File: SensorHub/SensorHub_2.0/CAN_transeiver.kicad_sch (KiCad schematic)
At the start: 4 parts, among them U3 TJA1051TK-3

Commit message: TCAN334
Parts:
- removed U3: TJA1051TK-3, Package_SON:HVSON-8-1EP_3x3mm_P0.65mm_EP1.6x2.4mm, symbol Interface_CAN_LIN:TJA1051TK-3
- added U9: TCAN334, Package_TO_SOT_SMD:TSOT-23-8_HandSoldering, symbol Interface_CAN_LIN:TCAN334
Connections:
- net +3.3V: now also U9.3 (VCC)
- net Can_H: now also U9.7 (CANH)
- net Can_L: now also U9.6 (CANL)
- net GND: now also U9.2 (GND), U9.5 (SHDN), U9.8 (STB)
- net RXD: now also U9.4 (RXD)
- net TXD: now also U9.1 (TXD)
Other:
- note removed: "CAN transceiver"
- moved on the sheet: C4, R13, R14

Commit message: TCAN334
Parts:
- removed U9: TCAN334, Package_TO_SOT_SMD:TSOT-23-8_HandSoldering, symbol Interface_CAN_LIN:TCAN334
- added U3: TCAN334, Package_TO_SOT_SMD:TSOT-23-8, symbol Interface_CAN_LIN:TCAN334
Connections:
- net +3.3V: now also U3.3 (VCC)
- net Can_H: now also U3.7 (CANH)
- net Can_L: now also U3.6 (CANL)
- net GND: now also U3.2 (GND), U3.5 (SHDN), U3.8 (STB)
- net RXD: now also U3.4 (RXD)
- net TXD: now also U3.1 (TXD)
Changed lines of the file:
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@@
+	)
+	(junction
+		(at 118.11 90.17)
+		(diameter 0)
+		(color 0 0 0 0)
+	)
+	(junction
+		(at 149.86 107.95)
+		(diameter 0)
+		(color 0 0 0 0)
 	)
 	(junction
@@
 		(color 0 0 0 0)
 	)
-	(junction
-		(at 149.86 107.95)
-		(diameter 0)
-		(color 0 0 0 0)
-	)
-	(junction
-		(at 118.11 90.17)
-		(diameter 0)
-		(color 0 0 0 0)
-	)
 	(wire
 		(pts
@@
 	(wire
 		(pts
+			(xy 149.86 107.95) (xy 149.86 113.03)
+		)
+		(stroke
+			(width 0)
+			(type default)
+		)
+	)
+	(wire
+		(pts
 			(xy 110.49 90.17) (xy 110.49 99.06)
 		)
@@
 	(wire
 		(pts
+			(xy 127 90.17) (xy 118.11 90.17)
+		)
+		(stroke
+			(width 0)
+			(type default)
+		)
+	)
+	(wire
+		(pts
+			(xy 110.49 116.84) (xy 110.49 106.68)
+		)
+		(stroke
+			(width 0)
+			(type default)
+		)
+	)
+	(wire
+		(pts
+			(xy 162.56 114.3) (xy 162.56 113.03)
+		)
+		(stroke
+			(width 0)
+			(type default)
+		)
+	)
+	(wire
+		(pts
 			(xy 149.86 105.41) (xy 149.86 107.95)
-		)
-		(stroke
-			(width 0)
-			(type default)
-		)
-	)
-	(wire
-		(pts
-			(xy 127 90.17) (xy 118.11 90.17)
-		)
-		(stroke
-			(width 0)
-			(type default)
-		)
-	)
-	(wire
-		(pts
-			(xy 149.86 107.95) (xy 149.86 113.03)
-		)
-		(stroke
-			(width 0)
-			(type default)
-		)
-	)
-	(wire
-		(pts
-			(xy 110.49 116.84) (xy 110.49 106.68)
-		)
-		(stroke
-			(width 0)
-			(type default)
-		)
-	)
-	(wire
-		(pts
-			(xy 162.56 114.3) (xy 162.56 113.03)
 		)
 		(stroke
@@
 	)
 	(symbol
-		(lib_id "Interface_CAN_LIN:TCAN334")
-		(at 162.56 102.87 0)
-		(unit 1)
-		(exclude_from_sim no)
-		(in_bom yes)
-		(on_board yes)
-		(dnp no)
-		(fields_autoplaced yes)
-		(property "Reference" "U9"
-			(at 164.7033 90.17 0)
-			(effects
-				(font
-					(size 1.27 1.27)
-				)
-				(justify left)
-			)
-		)
-		(property "Value" "TCAN334"
-			(at 164.7033 92.71 0)
-			(effects
-				(font
-					(size 1.27 1.27)
-				)
-				(justify left)
-			)
-		)
-		(property "Footprint" "Package_TO_SOT_SMD:TSOT-23-8_HandSoldering"
-			(at 162.56 115.57 0)
-			(effects
-				(font
-					(size 1.27 1.27)
-					(italic yes)
-				)
-				(hide yes)
-			)
-		)
-		(property "Datasheet" "http://www.ti.com/lit/ds/symlink/tcan337.pdf"
-			(at 162.56 102.87 0)
-			(effects
-				(font
-					(size 1.27 1.27)
-				)
-				(hide yes)
-			)
-		)
-		(property "Description" "High-Speed CAN Transceiver, 1Mbps, 3.3V supply, low power standby mode, shutdown mode, SOT-23-8/SOIC-8"
-			(at 162.56 102.87 0)
-			(effects
-				(font
-					(size 1.27 1.27)
-				)
-				(hide yes)
-			)
-		)
-		(pin "4"
-		)
-		(pin "7"
-		)
-		(pin "1"
-		)
-		(pin "5"
-		)
-		(pin "3"
-		)
-		(pin "6"
-		)
-		(pin "8"
-		)
-		(pin "2"
-		)
-		(instances
-			(project "SensorHub_2.0"
-				(path "/9668bc71-8924-498e-982f-628f3083c8b8/aeef27da-d3bb-47bb-8fd5-6871969d5416"
-					(reference "U9")
-					(unit 1)
-				)
-			)
-		)
-	)
-	(symbol
 		(lib_id "Device:R")
 		(at 118.11 102.87 0)
@@
 					(unit 1)
 				)
+			)
+		)
+	)
+	(symbol
+		(lib_id "Interface_CAN_LIN:TCAN334")
+		(at 162.56 102.87 0)
+		(unit 1)
+		(exclude_from_sim no)
+		(in_bom yes)
+		(on_board yes)
+		(dnp no)
+		(fields_autoplaced yes)
+		(property "Reference" "U3"
+			(at 164.7033 90.17 0)
+			(effects
+				(font
+					(size 1.27 1.27)
+				)
+				(justify left)
+			)
+		)
+		(property "Value" "TCAN334"
+			(at 164.7033 92.71 0)
+			(effects
+				(font
+					(size 1.27 1.27)
+				)
+				(justify left)
+			)
+		)
+		(property "Footprint" "Package_TO_SOT_SMD:TSOT-23-8"
+			(at 162.56 115.57 0)
+			(effects
+				(font
+					(size 1.27 1.27)
+					(italic yes)
+				)
+				(hide yes)
+			)
+		)
+		(property "Datasheet" "http://www.ti.com/lit/ds/symlink/tcan337.pdf"
+			(at 162.56 102.87 0)
+			(effects
+				(font
+					(size 1.27 1.27)
+				)
+				(hide yes)
+			)
+		)
+		(property "Description" "High-Speed CAN Transceiver, 1Mbps, 3.3V supply, low power standby mode, shutdown mode, SOT-23-8/SOIC-8"
+			(at 162.56 102.87 0)
+			(effects
+				(font
+					(size 1.27 1.27)
+				)
+				(hide yes)
+			)
+		)
+		(pin "3"
+		)
+		(pin "5"
+		)
+		(pin "1"
+		)
+		(pin "4"
+		)
+		(pin "2"
+		)
+		(pin "8"
+		)
+		(pin "7"
+		)
+		(pin "6"
+		)
+		(instances
+			(project "SensorHub_2.0"
+				(path "/9668bc71-8924-498e-982f-628f3083c8b8/aeef27da-d3bb-47bb-8fd5-6871969d5416"
+					(reference "U3")
+					(unit 1)
+				)

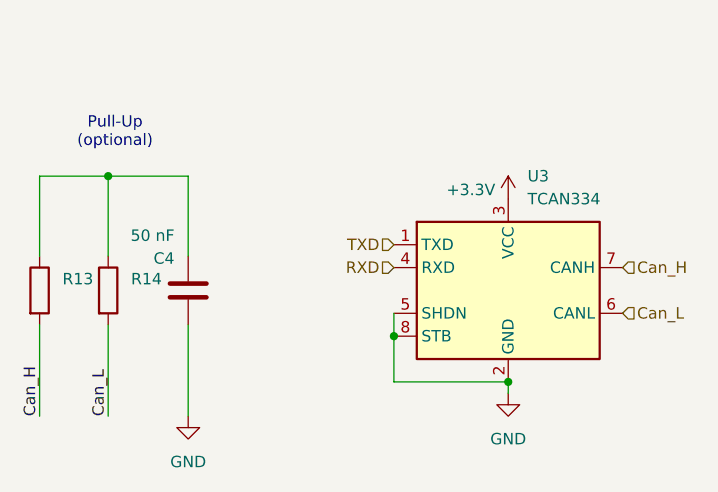
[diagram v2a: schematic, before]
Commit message: 32k oscillator
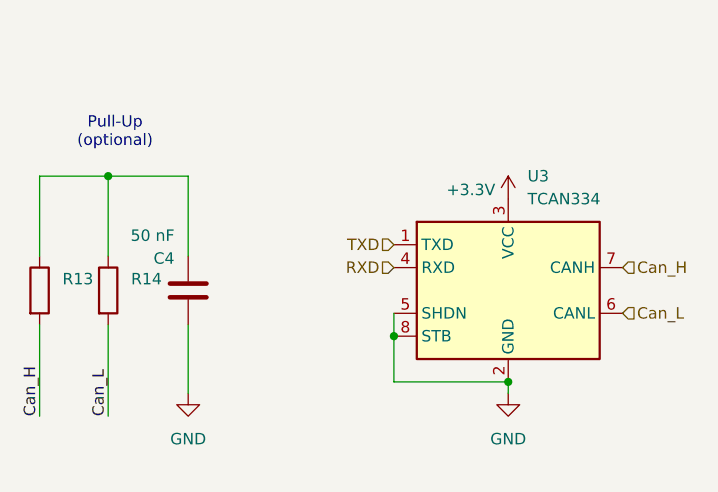
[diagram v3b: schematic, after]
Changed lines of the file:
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@@
 	(wire
 		(pts
-			(xy 127 106.68) (xy 127 116.84)
+			(xy 127 106.68) (xy 127 114.3)
 		)
 		(stroke
@@
 	(symbol
 		(lib_id "power:GND")
-		(at 127 116.84 0)
+		(at 127 114.3 0)
 		(unit 1)
 		(exclude_from_sim no)
@@
 		(fields_autoplaced yes)
 		(property "Reference" "#PWR016"
-			(at 127 123.19 0)
+			(at 127 120.65 0)
 			(effects
 				(font
@@
 		)
 		(property "Value" "GND"
-			(at 127 121.92 0)
+			(at 127 119.38 0)
 			(effects
 				(font
@@
 		)
 		(property "Footprint" ""
-			(at 127 116.84 0)
+			(at 127 114.3 0)
 			(effects
 				(font
@@
 		)
 		(property "Datasheet" ""
-			(at 127 116.84 0)
+			(at 127 114.3 0)
 			(effects
 				(font
@@
 		)
 		(property "Description" "Power symbol creates a global label with name \"GND\" , ground"
-			(at 127 116.84 0)
+			(at 127 114.3 0)
 			(effects
 				(font

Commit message: Vesrion 2
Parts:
- added R16: 10k, Resistor_SMD:R_0201_0603Metric, symbol Device:R
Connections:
- net GND: now also R16.1; no longer U3.5 (SHDN), U3.8 (STB)
- new net: R16.2, U3.5 (SHDN)
- new net STB: U3.8 (STB)
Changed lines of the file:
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@@
 		(color 0 0 0 0)
 	)
-	(junction
-		(at 149.86 107.95)
-		(diameter 0)
-		(color 0 0 0 0)
-	)
-	(junction
-		(at 162.56 113.03)
-		(diameter 0)
-		(color 0 0 0 0)
-	)
 	(wire
 		(pts
@@
 	(wire
 		(pts
-			(xy 149.86 107.95) (xy 149.86 113.03)
-		)
-		(stroke
-			(width 0)
-			(type default)
-		)
-	)
-	(wire
-		(pts
 			(xy 110.49 90.17) (xy 110.49 99.06)
 		)
@@
 	(wire
 		(pts
-			(xy 149.86 113.03) (xy 162.56 113.03)
+			(xy 144.78 105.41) (xy 149.86 105.41)
 		)
 		(stroke
@@
 	(wire
 		(pts
-			(xy 162.56 114.3) (xy 162.56 113.03)
-		)
-		(stroke
-			(width 0)
-			(type default)
-		)
-	)
-	(wire
-		(pts
-			(xy 149.86 105.41) (xy 149.86 107.95)
+			(xy 135.89 105.41) (xy 137.16 105.41)
 		)
 		(stroke
@@
 			)
 			(justify left bottom)
+		)
+	)
+	(hierarchical_label "STB"
+		(shape input)
+		(at 149.86 107.95 180)
+		(effects
+			(font
+				(size 1.27 1.27)
+			)
+			(justify right)
 		)
 	)
@@
 	)
 	(symbol
+		(lib_id "Device:R")
+		(at 140.97 105.41 90)
+		(unit 1)
+		(exclude_from_sim no)
+		(in_bom yes)
+		(on_board yes)
+		(dnp no)
+		(fields_autoplaced yes)
+		(property "Reference" "R16"
+			(at 140.97 99.06 90)
+			(effects
+				(font
+					(size 1.27 1.27)
+				)
+			)
+		)
+		(property "Value" "10k"
+			(at 140.97 101.6 90)
+			(effects
+				(font
+					(size 1.27 1.27)
+				)
+			)
+		)
+		(property "Footprint" "Resistor_SMD:R_0201_0603Metric"
+			(at 140.97 107.188 90)
+			(effects
+				(font
+					(size 1.27 1.27)
+				)
+				(hide yes)
+			)
+		)
+		(property "Datasheet" "~"
+			(at 140.97 105.41 0)
+			(effects
+				(font
+					(size 1.27 1.27)
+				)
+				(hide yes)
+			)
+		)
+		(property "Description" "Resistor"
+			(at 140.97 105.41 0)
+			(effects
+				(font
+					(size 1.27 1.27)
+				)
+				(hide yes)
+			)
+		)
+		(pin "1"
+		)
+		(pin "2"
+		)
+		(instances
+			(project "SensorHub_2.0"
+				(path "/9668bc71-8924-498e-982f-628f3083c8b8/aeef27da-d3bb-47bb-8fd5-6871969d5416"
+					(reference "R16")
+					(unit 1)
+				)
+			)
+		)
+	)
+	(symbol
 		(lib_id "power:GND")
-		(at 162.56 114.3 0)
+		(at 162.56 113.03 0)
 		(unit 1)
 		(exclude_from_sim no)
@@
 		(fields_autoplaced yes)
 		(property "Reference" "#PWR015"
-			(at 162.56 120.65 0)
+			(at 162.56 119.38 0)
 			(effects
 				(font
@@
 		)
 		(property "Value" "GND"
-			(at 162.56 119.38 0)
+			(at 162.56 118.11 0)
 			(effects
 				(font
@@
 		)
 		(property "Footprint" ""
-			(at 162.56 114.3 0)
+			(at 162.56 113.03 0)
 			(effects
 				(font
@@
 		)
 		(property "Datasheet" ""
-			(at 162.56 114.3 0)
+			(at 162.56 113.03 0)
 			(effects
 				(font
@@
 		)
 		(property "Description" "Power symbol creates a global label with name \"GND\" , ground"
-			(at 162.56 114.3 0)
+			(at 162.56 113.03 0)
 			(effects
 				(font
@@
 					(unit 1)
 				)
+			)
+		)
+	)
+	(symbol
+		(lib_id "power:GND")
+		(at 135.89 105.41 0)
+		(unit 1)
+		(exclude_from_sim no)
+		(in_bom yes)
+		(on_board yes)
+		(dnp no)
+		(fields_autoplaced yes)
+		(property "Reference" "#PWR03"
+			(at 135.89 111.76 0)
+			(effects
+				(font
+					(size 1.27 1.27)
+				)
+				(hide yes)
+			)
+		)
+		(property "Value" "GND"
+			(at 135.89 110.49 0)
+			(effects
+				(font
+					(size 1.27 1.27)
+				)
+			)
+		)
+		(property "Footprint" ""
+			(at 135.89 105.41 0)
+			(effects
+				(font
+					(size 1.27 1.27)
+				)
+				(hide yes)
+			)
+		)
+		(property "Datasheet" ""
+			(at 135.89 105.41 0)
+			(effects
+				(font
+					(size 1.27 1.27)
+				)
+				(hide yes)
+			)
+		)
+		(property "Description" "Power symbol creates a global label with name \"GND\" , ground"
+			(at 135.89 105.41 0)
+			(effects
+				(font
+					(size 1.27 1.27)
+				)
+				(hide yes)
+			)
+		)
+		(pin "1"
+		)
+		(instances
+			(project "SensorHub_2.0"
+				(path "/9668bc71-8924-498e-982f-628f3083c8b8/aeef27da-d3bb-47bb-8fd5-6871969d5416"
+					(reference "#PWR03")
+					(unit 1)
+				)

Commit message: MPN + CC fix
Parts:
- U3: MPN (none) -> TCAN334GDCNT
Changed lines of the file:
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@@
+			)
+		)
+		(property "MPN" "TCAN334GDCNT "
+			(at 162.56 102.87 0)
+			(effects
+				(font
+					(size 1.27 1.27)
+				)
+				(hide yes)
 			)
 		)

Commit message: pcb fix
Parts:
- R13, R14, R16: footprint Resistor_SMD:R_0201_0603Metric -> Resistor_SMD:R_0402_1005Metric
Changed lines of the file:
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@@
 			)
 		)
-		(property "Footprint" "Resistor_SMD:R_0201_0603Metric"
+		(property "Footprint" "Resistor_SMD:R_0402_1005Metric"
 			(at 116.332 102.87 90)
 			(effects
@@
 			)
 		)
-		(property "Footprint" "Resistor_SMD:R_0201_0603Metric"
+		(property "Footprint" "Resistor_SMD:R_0402_1005Metric"
 			(at 108.712 102.87 90)
 			(effects
@@
 			)
 		)
-		(property "Footprint" "Resistor_SMD:R_0201_0603Metric"
+		(property "Footprint" "Resistor_SMD:R_0402_1005Metric"
 			(at 140.97 107.188 90)
 			(effects

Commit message: v 2.3
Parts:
- R13, R14, R16: footprint Resistor_SMD:R_0402_1005Metric -> Resistor_SMD:R_0603_1608Metric
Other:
- note added: "terminating R (optional)"
- note removed: "Pull-Up (optional)"
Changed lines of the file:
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@@
 	(generator_version "9.0")
 	(paper "A4")
-	(text "Pull-Up\n(optional)"
+	(text "terminating R\n(optional)"
 		(exclude_from_sim no)
 		(at 118.872 85.344 0)
@@
 			)
 		)
-		(property "Footprint" "Resistor_SMD:R_0402_1005Metric"
+		(property "Footprint" "Resistor_SMD:R_0603_1608Metric"
 			(at 116.332 102.87 90)
 			(effects
@@
 			)
 		)
-		(property "Footprint" "Resistor_SMD:R_0402_1005Metric"
+		(property "Footprint" "Resistor_SMD:R_0603_1608Metric"
 			(at 108.712 102.87 90)
 			(effects
@@
 			)
 		)
-		(property "Footprint" "Resistor_SMD:R_0402_1005Metric"
+		(property "Footprint" "Resistor_SMD:R_0603_1608Metric"
 			(at 140.97 107.188 90)
 			(effects
